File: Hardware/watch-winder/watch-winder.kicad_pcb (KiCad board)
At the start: 4 copper layers, 50 x 35 mm, 56 parts, among them J1 SWD, J2 UART, J3 MOT, J4 SYNC0, J5 SYNC1, J6 PWR, SW1 SW_Push, SW2 SW_Push, SW3 SW_Push, U1 STM32F030K6Tx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

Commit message: routing
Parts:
- moved R7 0.80 mm to (197.2, 140.8)
- moved R8 0.80 mm to (197.2, 142.7)
- moved R9 0.80 mm to (197.2, 144.6)
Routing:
- net +5V: track 0.00 -> 59.1 mm
- net GND: track 0.00 -> 37.7 mm, vias 0 -> 21
- net /MOT3: track 0.00 -> 34.5 mm, vias 0 -> 2
- net /SYNC0: track 0.00 -> 34.2 mm, vias 0 -> 2
- net Net-(J3-Pin_5): track 0.00 -> 33.2 mm
- net /LED2: track 0.00 -> 31.3 mm, vias 0 -> 2
- net Net-(J4-Pin_2): track 0.00 -> 31.2 mm, vias 0 -> 2
- net /SYNC1: track 0.00 -> 30.7 mm, vias 0 -> 2
- net Net-(J3-Pin_4): track 0.00 -> 29.7 mm
- net Net-(J5-Pin_2): track 0.00 -> 27.3 mm, vias 0 -> 1
- net /LED1: track 0.00 -> 26.6 mm, vias 0 -> 2
- net /MOT1: track 0.00 -> 26.4 mm, vias 0 -> 1
- net /MOT2: track 0.00 -> 26.0 mm, vias 0 -> 1
- net Net-(J3-Pin_3): track 0.00 -> 26.0 mm
- net /BUT0: track 0.00 -> 25.3 mm, vias 0 -> 1
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- added copper zone on B.Cu, net +3V3
- added copper zone on F.Cu, net +3V3

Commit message: remove drc errors
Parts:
- moved R6 2.12 mm to (200.5, 146.1), turned to 90 degrees
- moved REF** 0.71 mm to (206.5, 146.5)
- moved R5 0.57 mm to (202.4, 146.1), turned to 90 degrees
- moved D1 0.40 mm to (198.5, 147.4)
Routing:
- net /UART_RX: track 19.5 -> 13.6 mm
- net Net-(J2-Pin_3): track 5.96 -> 8.67 mm
- net +3V3: track 13.7 -> 15.6 mm, vias 2 -> 6
- net /UART_TX: track 16.5 -> 17.7 mm
- net GND: track 37.7 -> 36.6 mm
- net /LED0: track 22.4 -> 23.2 mm
- net /SWD_IO: track 14.0 -> 14.7 mm

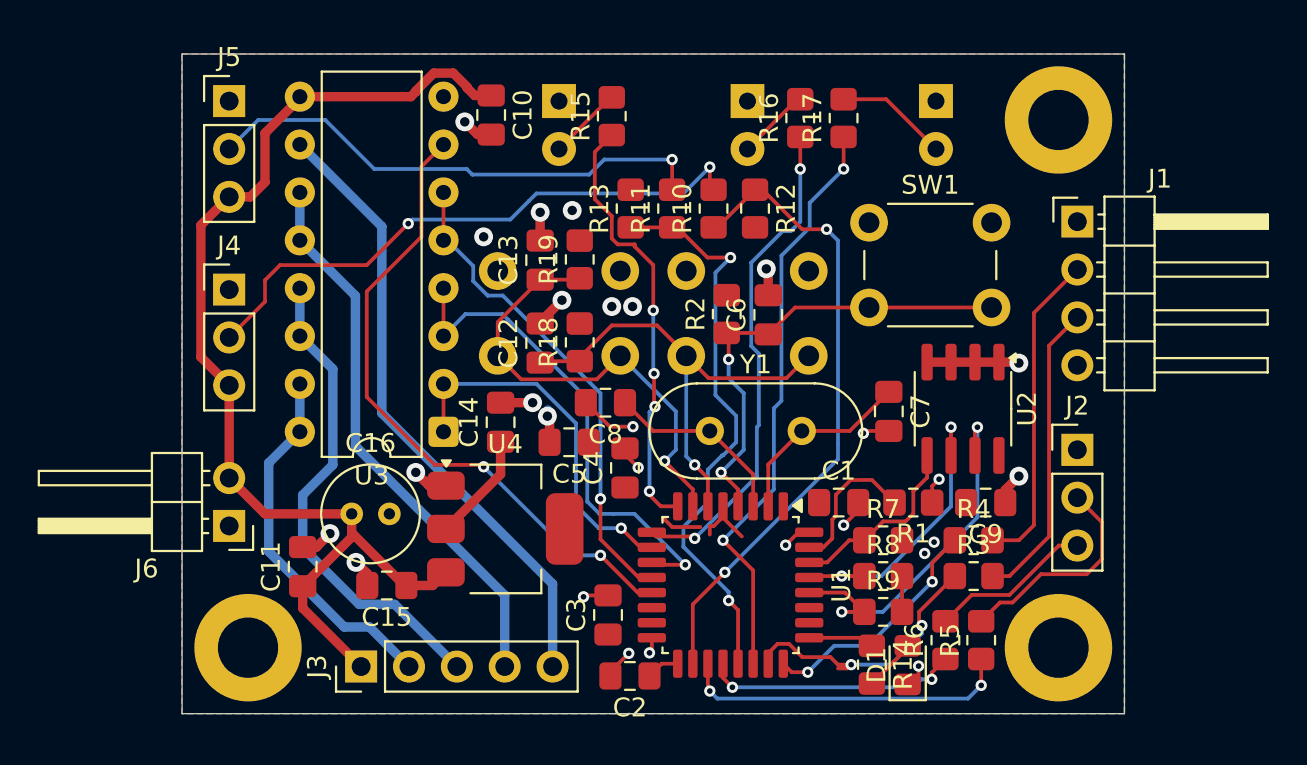
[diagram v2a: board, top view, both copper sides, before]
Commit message: add ground vias near signal vias
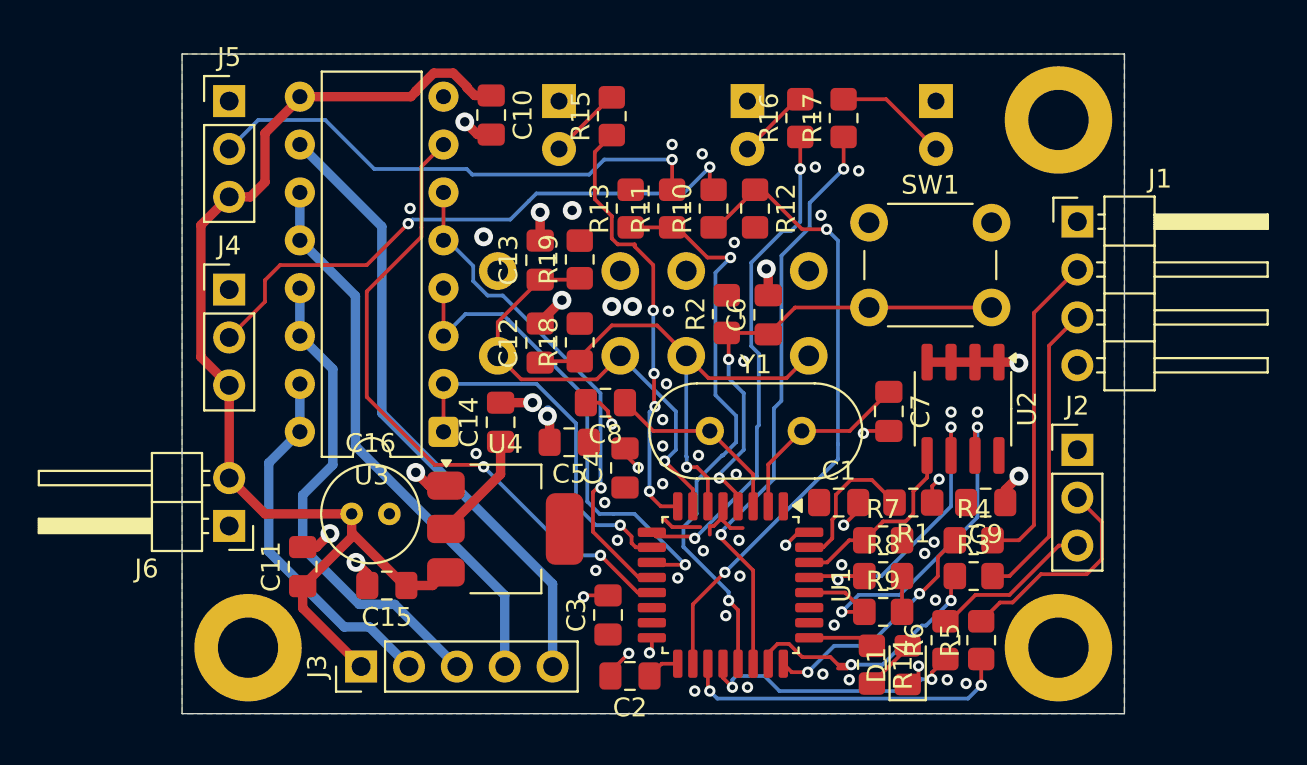
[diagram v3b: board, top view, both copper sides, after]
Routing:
- net GND: track 36.6 -> 35.7 mm, vias 21 -> 56
- net /UART_RX: track 13.6 -> 14.5 mm
- net +3V3: track 15.6 -> 16.1 mm

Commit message: add power vias
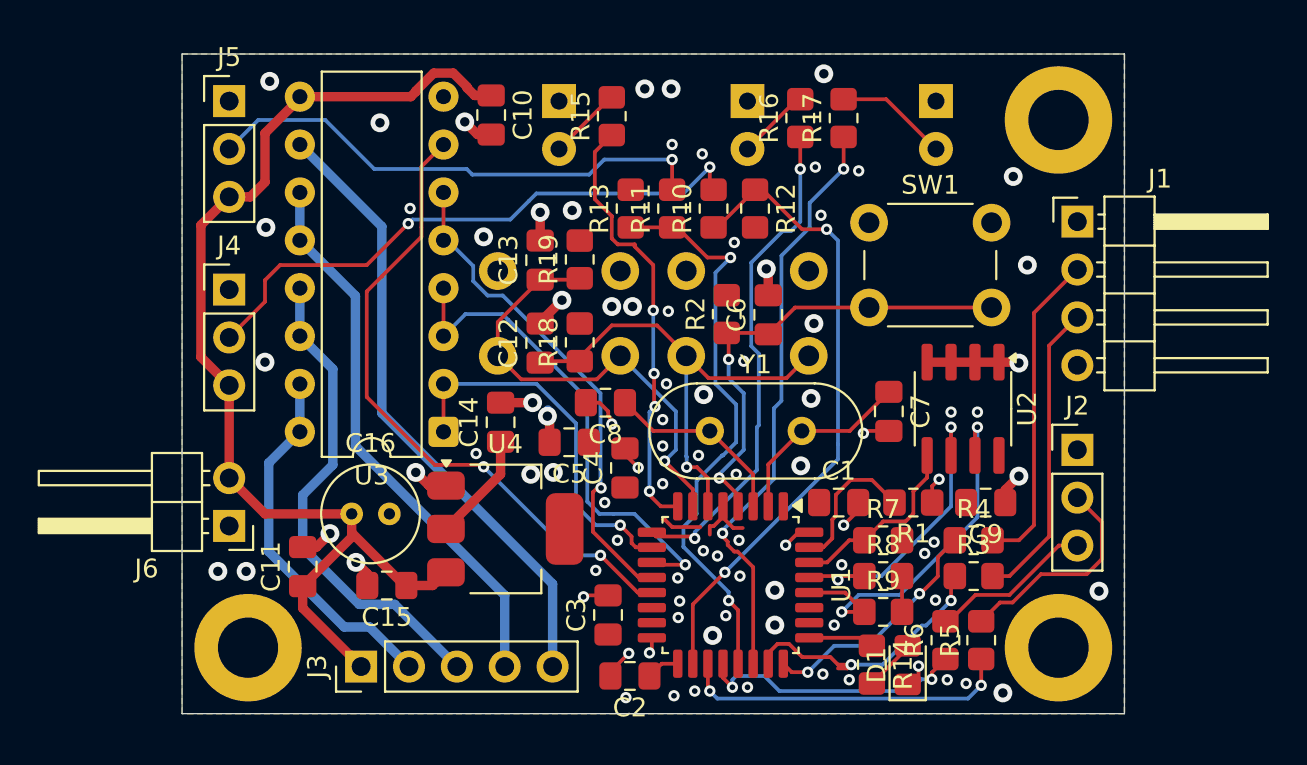
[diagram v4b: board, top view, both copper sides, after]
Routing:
- net +3V3: track 16.1 -> 15.4 mm, vias 6 -> 33
